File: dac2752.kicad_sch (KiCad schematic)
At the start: 24 parts, among them U30 LTC2752B, U301 OPA2197D, U31 OPA2189DGK, U32 OPA2388DGK, U34 OPA2388DGK

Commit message: Progress checkin.  About to redo FDA feedback again.
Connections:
- net Alt: now also R316.1; no longer R316.2
- net Force: now also C303.1; no longer C303.2
- net GND: now also R309.2; no longer R309.1
- net IOUT1: now also C303.2; no longer C303.1
- net at C304.2, U32.6 (-): now also R309.1; no longer R309.2
- net at C311.1, R315.1, U31.3 (+): now also R316.2; no longer R316.1
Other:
- moved on the sheet: C303, R309, R316
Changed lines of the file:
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@@
 	)
 	(junction
-		(at 170.18 118.11)
+		(at 144.78 81.28)
 		(diameter 0)
 		(color 0 0 0 0)
 	)
 	(junction
-		(at 110.49 81.28)
+		(at 170.18 118.11)
 		(diameter 0)
 		(color 0 0 0 0)
 	)
 	(junction
-		(at 153.67 100.33)
+		(at 110.49 81.28)
 		(diameter 0)
 		(color 0 0 0 0)
 	)
 	(junction
-		(at 102.87 101.6)
+		(at 153.67 100.33)
 		(diameter 0)
 		(color 0 0 0 0)
 	)
 	(junction
-		(at 144.78 81.28)
+		(at 102.87 101.6)
 		(diameter 0)
 		(color 0 0 0 0)
@@
 	)
 	(junction
-		(at 144.78 88.9)
-		(diameter 0)
-		(color 0 0 0 0)
-	)
-	(junction
 		(at 168.91 93.98)
 		(diameter 0)
@@
 	)
 	(junction
+		(at 144.78 88.9)
+		(diameter 0)
+		(color 0 0 0 0)
+	)
+	(junction
 		(at 73.66 76.2)
 		(diameter 0)
@@
 	(wire
 		(pts
-			(xy 144.78 81.28) (xy 194.31 81.28)
+			(xy 72.39 73.66) (xy 73.66 73.66)
 		)
 		(stroke
@@
 	(wire
 		(pts
-			(xy 72.39 73.66) (xy 73.66 73.66)
+			(xy 73.66 73.66) (xy 73.66 76.2)
 		)
 		(stroke
@@
 	(wire
 		(pts
-			(xy 73.66 73.66) (xy 73.66 76.2)
+			(xy 80.01 81.28) (xy 80.01 86.36)
 		)
 		(stroke
@@
 	(wire
 		(pts
-			(xy 80.01 81.28) (xy 80.01 86.36)
+			(xy 63.5 76.2) (xy 64.77 76.2)
 		)
 		(stroke
@@
 	(wire
 		(pts
-			(xy 63.5 76.2) (xy 64.77 76.2)
+			(xy 62.23 99.06) (xy 62.23 93.98)
 		)
 		(stroke
@@
 	(wire
 		(pts
-			(xy 62.23 99.06) (xy 62.23 93.98)
+			(xy 66.04 110.49) (xy 62.23 110.49)
 		)
 		(stroke
@@
 	(wire
 		(pts
-			(xy 66.04 110.49) (xy 62.23 110.49)
+			(xy 144.78 88.9) (xy 153.67 88.9)
 		)
 		(stroke
@@
 	(wire
 		(pts
+			(xy 144.78 81.28) (xy 194.31 81.28)
+		)
+		(stroke
+			(width 0)
+			(type default)
+		)
+	)
+	(wire
+		(pts
 			(xy 102.87 93.98) (xy 110.49 93.98)
 		)
@@
 	(wire
 		(pts
-			(xy 144.78 88.9) (xy 153.67 88.9)
-		)
-		(stroke
-			(width 0)
-			(type default)
-		)
-	)
-	(wire
-		(pts
 			(xy 102.87 101.6) (xy 102.87 110.49)
 		)
@@
 		(lib_id "Device:C")
 		(at 170.18 114.3 0)
-		(mirror y)
 		(unit 1)
 		(exclude_from_sim no)
@@
 					(size 1.27 1.27)
 				)
-				(justify right)
+				(justify left)
 			)
 		)
@@
 					(size 1.27 1.27)
 				)
-				(justify right top)
+				(justify left top)
 			)
 		)
 		(property "Footprint" "Capacitor_SMD:C_0402_1005Metric"
-			(at 169.2148 118.11 0)
+			(at 171.1452 118.11 0)
 			(effects
 				(font
@@
 		(dnp no)
 		(property "Reference" "R303"
-			(at 82.55 106.172 90)
+			(at 82.55 102.108 90)
 			(effects
 				(font
@@
 		(lib_id "Device:R")
 		(at 57.15 110.49 270)
-		(mirror x)
 		(unit 1)
 		(exclude_from_sim no)
@@
 		(dnp no)
 		(property "Reference" "R301"
-			(at 57.15 108.458 90)
+			(at 57.15 112.522 90)
 			(effects
 				(font
@@
 		)
 		(property "Footprint" "Resistor_SMD:R_0402_1005Metric"
-			(at 57.15 112.268 90)
+			(at 57.15 108.712 90)
 			(effects
 				(font
@@
 		(lib_id "Device:C")
 		(at 185.42 114.3 0)
-		(mirror y)
 		(unit 1)
 		(exclude_from_sim no)
@@
 					(size 1.27 1.27)
 				)
-				(justify left)
+				(justify right)
 			)
 		)
@@
 					(size 1.27 1.27)
 				)
-				(justify left top)
+				(justify right top)
 			)
 		)
 		(property "Footprint" "Capacitor_SMD:C_0402_1005Metric"
-			(at 184.4548 118.11 0)
+			(at 186.3852 118.11 0)
 			(effects
 				(font
@@
 		(lib_id "Device:C")
 		(at 69.85 110.49 270)
-		(mirror x)
 		(unit 1)
 		(exclude_from_sim no)
@@
 		)
 		(property "Footprint" "Capacitor_SMD:C_0603_1608Metric"
-			(at 66.04 109.5248 0)
+			(at 66.04 111.4552 0)
 			(effects
 				(font
@@
 	(symbol
 		(lib_id "Device:C")
-		(at 144.78 85.09 180)
+		(at 144.78 85.09 0)
 		(unit 1)
 		(exclude_from_sim no)
@@
 		(dnp no)
 		(property "Reference" "C303"
-			(at 144.78 83.058 0)
+			(at 144.78 82.804 0)
 			(effects
 				(font
@@
 		)
 		(property "Value" "330p"
-			(at 144.78 83.058 0)
+			(at 144.78 82.804 0)
 			(effects
 				(font
@@
 		)
 		(property "Footprint" "Capacitor_SMD:C_0603_1608Metric"
-			(at 143.8148 81.28 0)
+			(at 145.7452 88.9 0)
 			(effects
 				(font
@@
 	(symbol
 		(lib_id "Device:R")
-		(at 68.58 73.66 270)
-		(mirror x)
+		(at 68.58 73.66 90)
 		(unit 1)
 		(exclude_from_sim no)
@@
 		(lib_id "Device:C")
 		(at 170.18 121.92 0)
-		(mirror y)
 		(unit 1)
 		(exclude_from_sim no)
@@
 					(size 1.27 1.27)
 				)
-				(justify right)
+				(justify left)
 			)
 		)
@@
 					(size 1.27 1.27)
 				)
-				(justify right top)
+				(justify left top)
 			)
 		)
 		(property "Footprint" "Capacitor_SMD:C_0402_1005Metric"
-			(at 169.2148 125.73 0)
+			(at 171.1452 125.73 0)
 			(effects
 				(font
@@
 	(symbol
 		(lib_id "Device:R")
-		(at 153.67 105.41 180)
+		(at 153.67 105.41 0)
 		(unit 1)
 		(exclude_from_sim no)
@@
 		)
 		(property "Footprint" "Resistor_SMD:R_0402_1005Metric"
-			(at 155.448 105.41 90)
+			(at 151.892 105.41 90)
 			(effects
 				(font
@@
 		(lib_id "Device:R")
 		(at 173.99 93.98 270)
-		(mirror x)
 		(unit 1)
 		(exclude_from_sim no)
@@
 		)
 		(property "Footprint" "Resistor_SMD:R_0402_1005Metric"
-			(at 173.99 95.758 90)
+			(at 173.99 92.202 90)
 			(effects
 				(font
@@
 		(lib_id "Device:R")
 		(at 68.58 76.2 270)
-		(mirror x)
 		(unit 1)
 		(exclude_from_sim no)
@@
 		)
 		(property "Footprint" "Resistor_SMD:R_0603_1608Metric"
-			(at 68.58 77.978 90)
+			(at 68.58 74.422 90)
 			(effects
 				(font
@@
 		(lib_id "Device:C")
 		(at 161.29 100.33 270)
-		(mirror x)
 		(unit 1)
 		(exclude_from_sim no)
@@
 		)
 		(property "Footprint" "Capacitor_SMD:C_0603_1608Metric"
-			(at 157.48 99.3648 0)
+			(at 157.48 101.2952 0)
 			(effects
 				(font
@@
 		(lib_id "Device:C")
 		(at 185.42 121.92 0)
-		(mirror y)
 		(unit 1)
 		(exclude_from_sim no)
@@
 					(size 1.27 1.27)
 				)
-				(justify left)
+				(justify right)
 			)
 		)
@@
 					(size 1.27 1.27)
 				)
-				(justify left top)
+				(justify right top)
 			)
 		)
 		(property "Footprint" "Capacitor_SMD:C_0402_1005Metric"
-			(at 184.4548 125.73 0)
+			(at 186.3852 125.73 0)
 			(effects
 				(font

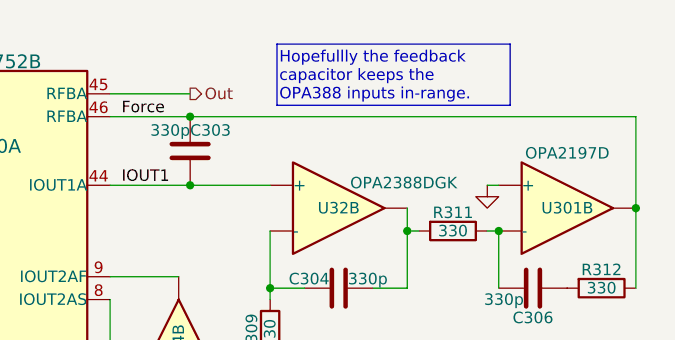
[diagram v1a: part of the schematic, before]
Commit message: Start to place within physical board size.
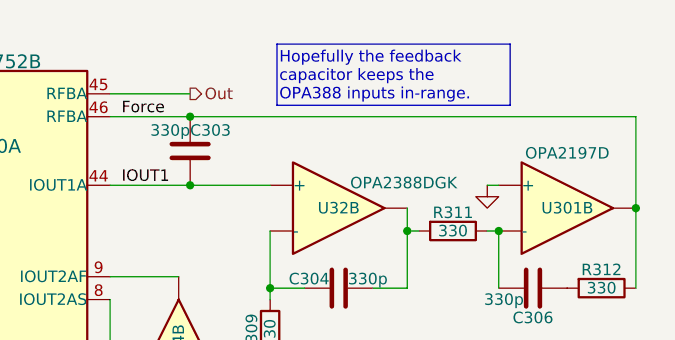
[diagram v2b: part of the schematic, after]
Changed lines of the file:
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@@
 	(generator_version "9.0")
 	(paper "A4")
-	(text_box "Hopefullly the feedback capacitor keeps the OPA388 inputs in-range."
+	(text_box "Hopefully the feedback capacitor keeps the OPA388 inputs in-range."
 		(exclude_from_sim no)
 		(at 154.4319 73.2099 0)

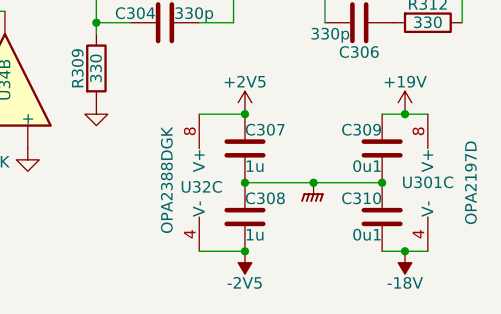
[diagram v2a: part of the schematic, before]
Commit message: Power mostly routed
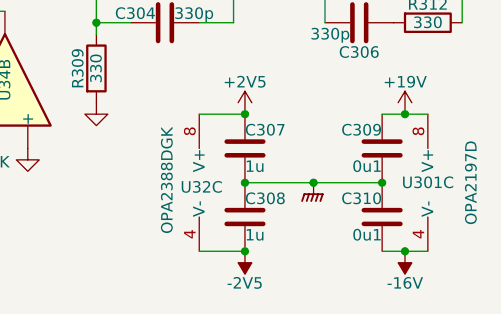
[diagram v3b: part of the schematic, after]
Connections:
- net -18V renamed -16V
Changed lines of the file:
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@@
 				)
 				(path "/b054cef4-39e3-49d8-aff0-7ba5a206c187/aeb3a378-4287-41b1-9e33-8dbd035c4d66"
-					(reference "C367")
+					(reference "C366")
 					(unit 1)
 				)
@@
 				)
 				(path "/b054cef4-39e3-49d8-aff0-7ba5a206c187/aeb3a378-4287-41b1-9e33-8dbd035c4d66"
-					(reference "C369")
+					(reference "C368")
 					(unit 1)
 				)
@@
 				)
 				(path "/b054cef4-39e3-49d8-aff0-7ba5a206c187/aeb3a378-4287-41b1-9e33-8dbd035c4d66"
-					(reference "C366")
+					(reference "C365")
 					(unit 1)
 				)
@@
 				)
 				(path "/b054cef4-39e3-49d8-aff0-7ba5a206c187/aeb3a378-4287-41b1-9e33-8dbd035c4d66"
-					(reference "C368")
+					(reference "C367")
 					(unit 1)
 				)
@@
 				)
 				(path "/b054cef4-39e3-49d8-aff0-7ba5a206c187/aeb3a378-4287-41b1-9e33-8dbd035c4d66"
-					(reference "C370")
+					(reference "C369")
 					(unit 1)
 				)
@@
 	)
 	(symbol
-		(lib_id "External:-18V")
+		(lib_id "Parts:-16V")
 		(at 187.96 125.73 0)
 		(mirror y)
@@
 			)
 		)
-		(property "Value" "-18V"
+		(property "Value" "-16V"
 			(at 187.96 129.286 0)
 			(do_not_autoplace yes)
@@
 			)
 		)
-		(property "Description" "Power symbol creates a global label with name \"-18V\""
+		(property "Description" "Power symbol creates a global label with name \"-16V\""
 			(at 187.96 125.73 0)
 			(effects

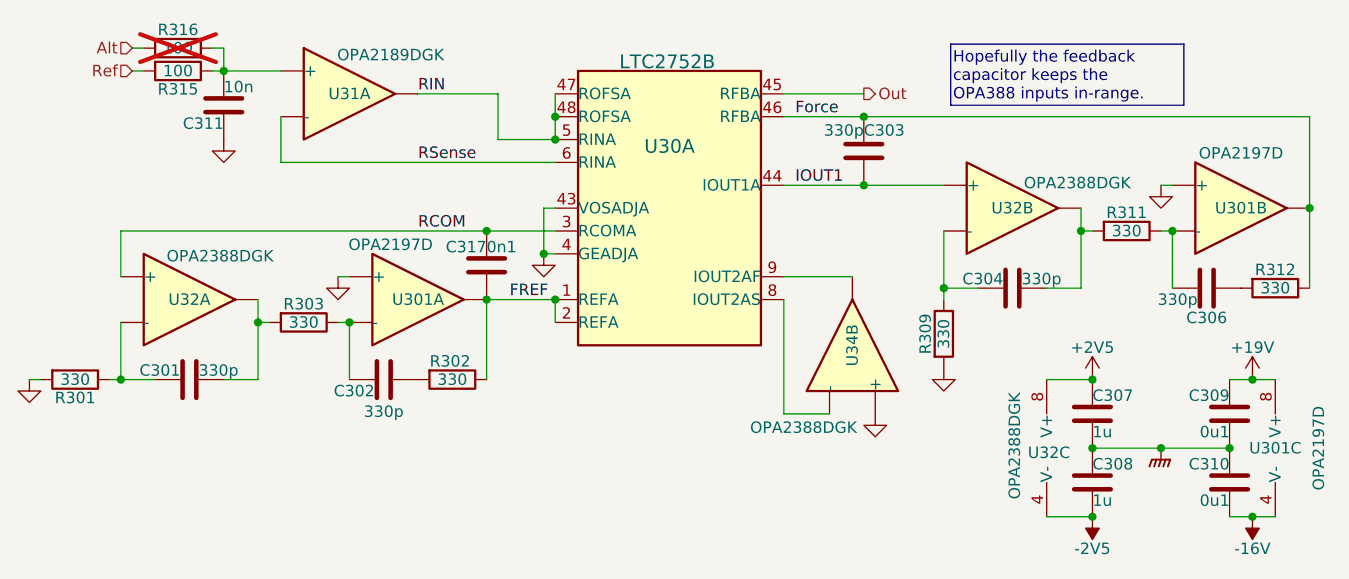
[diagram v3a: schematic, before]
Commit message: Nearly all routed.  Repinning FDA resistors.
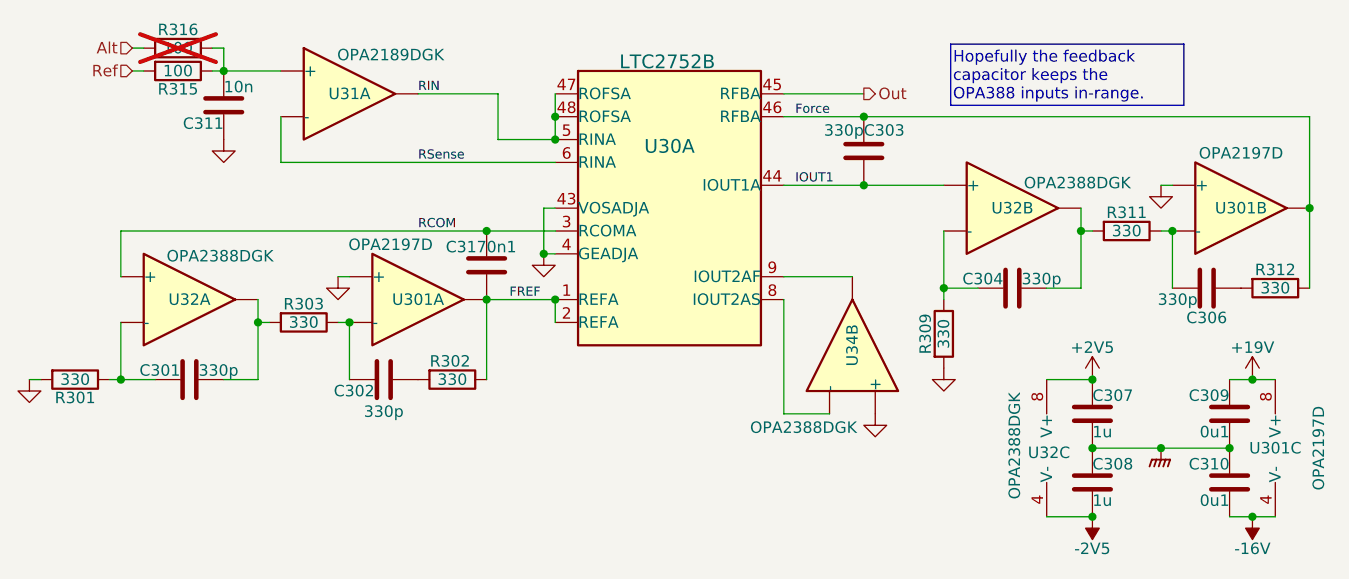
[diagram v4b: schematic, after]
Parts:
- C317: footprint Capacitor_SMD:C_0402_1005Metric -> Capacitor_SMD:C_0603_1608Metric; LCSC C1546 -> (none)
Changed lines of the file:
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@@
 		(effects
 			(font
-				(size 1.27 1.27)
+				(size 1.016 1.016)
 			)
 			(justify left bottom)
@@
 		(effects
 			(font
-				(size 1.27 1.27)
+				(size 1.016 1.016)
 			)
 			(justify left bottom)
@@
 		(effects
 			(font
-				(size 1.27 1.27)
+				(size 1.016 1.016)
 			)
 			(justify left bottom)
@@
 		(effects
 			(font
-				(size 1.27 1.27)
+				(size 1.016 1.016)
 			)
 			(justify left bottom)
@@
 		(effects
 			(font
-				(size 1.27 1.27)
+				(size 1.016 1.016)
 			)
 			(justify left bottom)
@@
 		(effects
 			(font
-				(size 1.27 1.27)
+				(size 1.016 1.016)
 			)
 			(justify left bottom)
@@
 			)
 		)
-		(property "Footprint" "Capacitor_SMD:C_0402_1005Metric"
+		(property "Footprint" "Capacitor_SMD:C_0603_1608Metric"
 			(at 103.8352 101.6 0)
 			(effects
@@
 			)
 		)
-		(property "LCSC" "C1546"
+		(property "LCSC" ""
 			(at 102.87 97.79 0)
 			(effects

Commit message: DRC update.  Repin ADC.  De-crack the S/H ground.
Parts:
- added R304: 100, Resistor_SMD:R_0402_1005Metric, symbol Device:R
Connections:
- net Force: now also R304.2; no longer U30.46 (RFBA)
- new net: R304.1, U30.46 (RFBA)
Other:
- moved on the sheet: C303
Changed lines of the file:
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@@
-	)
-	(junction
-		(at 144.78 81.28)
-		(diameter 0)
-		(color 0 0 0 0)
 	)
 	(junction
@@
 	)
 	(junction
+		(at 152.4 88.9)
+		(diameter 0)
+		(color 0 0 0 0)
+	)
+	(junction
+		(at 152.4 81.28)
+		(diameter 0)
+		(color 0 0 0 0)
+	)
+	(junction
 		(at 102.87 101.6)
 		(diameter 0)
@@
 	)
 	(junction
-		(at 144.78 88.9)
-		(diameter 0)
-		(color 0 0 0 0)
-	)
-	(junction
 		(at 73.66 76.2)
 		(diameter 0)
@@
 	(wire
 		(pts
-			(xy 144.78 88.9) (xy 153.67 88.9)
-		)
-		(stroke
-			(width 0)
-			(type default)
-		)
-	)
-	(wire
-		(pts
 			(xy 187.96 125.73) (xy 185.42 125.73)
 		)
@@
 	(wire
 		(pts
-			(xy 144.78 81.28) (xy 194.31 81.28)
-		)
-		(stroke
-			(width 0)
-			(type default)
-		)
-	)
-	(wire
-		(pts
 			(xy 102.87 93.98) (xy 110.49 93.98)
 		)
@@
 	(wire
 		(pts
-			(xy 135.89 81.28) (xy 144.78 81.28)
+			(xy 135.89 81.28) (xy 142.24 81.28)
 		)
 		(stroke
@@
 	(wire
 		(pts
+			(xy 152.4 88.9) (xy 153.67 88.9)
+		)
+		(stroke
+			(width 0)
+			(type default)
+		)
+	)
+	(wire
+		(pts
 			(xy 135.89 78.74) (xy 144.78 78.74)
 		)
@@
 	(wire
 		(pts
+			(xy 152.4 81.28) (xy 194.31 81.28)
+		)
+		(stroke
+			(width 0)
+			(type default)
+		)
+	)
+	(wire
+		(pts
 			(xy 52.07 110.49) (xy 53.34 110.49)
 		)
@@
 	(wire
 		(pts
-			(xy 135.89 88.9) (xy 144.78 88.9)
+			(xy 135.89 88.9) (xy 152.4 88.9)
 		)
 		(stroke
@@
 		(pts
 			(xy 165.1 110.49) (xy 170.18 110.49)
+		)
+		(stroke
+			(width 0)
+			(type default)
+		)
+	)
+	(wire
+		(pts
+			(xy 149.86 81.28) (xy 152.4 81.28)
 		)
 		(stroke
@@
 	)
 	(label "Force"
-		(at 137.16 81.28 0)
+		(at 181.61 81.28 0)
 		(effects
 			(font
@@
 				(path "/b054cef4-39e3-49d8-aff0-7ba5a206c187/f2e682f2-52ca-4ed0-8a7d-aeb09fbc9914"
 					(reference "R302")
+					(unit 1)
+				)
+			)
+		)
+	)
+	(symbol
+		(lib_id "Device:R")
+		(at 146.05 81.28 90)
+		(unit 1)
+		(exclude_from_sim no)
+		(in_bom yes)
+		(on_board yes)
+		(dnp no)
+		(property "Reference" "R304"
+			(at 146.05 83.312 90)
+			(effects
+				(font
+					(size 1.27 1.27)
+				)
+			)
+		)
+		(property "Value" "100"
+			(at 146.05 81.28 90)
+			(effects
+				(font
+					(size 1.27 1.27)
+				)
+			)
+		)
+		(property "Footprint" "Resistor_SMD:R_0402_1005Metric"
+			(at 146.05 83.058 90)
+			(effects
+				(font
+					(size 1.27 1.27)
+				)
+				(hide yes)
+			)
+		)
+		(property "Datasheet" "~"
+			(at 146.05 81.28 0)
+			(effects
+				(font
+					(size 1.27 1.27)
+				)
+				(hide yes)
+			)
+		)
+		(property "Description" "Resistor"
+			(at 146.05 81.28 0)
+			(effects
+				(font
+					(size 1.27 1.27)
+				)
+				(hide yes)
+			)
+		)
+		(property "LCSC" "C25076"
+			(at 146.05 81.28 90)
+			(effects
+				(font
+					(size 1.27 1.27)
+				)
+				(hide yes)
+			)
+		)
+		(property "Stock" ""
+			(at 146.05 81.28 90)
+			(effects
+				(font
+					(size 1.27 1.27)
+				)
+				(hide yes)
+			)
+		)
+		(pin "2"
+		)
+		(pin "1"
+		)
+		(instances
+			(project "lincal"
+				(path "/b054cef4-39e3-49d8-aff0-7ba5a206c187/361a423f-d05f-4f8b-bc28-600b62434109"
+					(reference "R324")
+					(unit 1)
+				)
+				(path "/b054cef4-39e3-49d8-aff0-7ba5a206c187/460d889b-fb9b-4b3e-8128-6fba79ce7ab4"
+					(reference "R344")
+					(unit 1)
+				)
+				(path "/b054cef4-39e3-49d8-aff0-7ba5a206c187/aeb3a378-4287-41b1-9e33-8dbd035c4d66"
+					(reference "R364")
+					(unit 1)
+				)
+				(path "/b054cef4-39e3-49d8-aff0-7ba5a206c187/f2e682f2-52ca-4ed0-8a7d-aeb09fbc9914"
+					(reference "R304")
 					(unit 1)
 				)
@@
 	(symbol
 		(lib_id "Device:C")
-		(at 144.78 85.09 0)
+		(at 152.4 85.09 0)
 		(unit 1)
 		(exclude_from_sim no)
@@
 		(dnp no)
 		(property "Reference" "C303"
-			(at 144.78 82.804 0)
+			(at 152.4 82.804 0)
 			(effects
 				(font
@@
 		)
 		(property "Value" "330p"
-			(at 144.78 82.804 0)
+			(at 152.4 87.122 0)
 			(effects
 				(font
@@
 		)
 		(property "Footprint" "Capacitor_SMD:C_0603_1608Metric"
-			(at 145.7452 88.9 0)
+			(at 153.3652 88.9 0)
 			(effects
 				(font
@@
 		)
 		(property "Datasheet" "C0G, 50V"
-			(at 144.78 85.09 0)
+			(at 152.4 85.09 0)
 			(effects
 				(font
@@
 		)
 		(property "Description" "Unpolarized capacitor"
-			(at 144.78 85.09 0)
+			(at 152.4 85.09 0)
 			(effects
 				(font
@@
 		)
 		(property "LCSC" "C1664"
-			(at 144.78 85.09 0)
+			(at 152.4 85.09 0)
 			(effects
 				(font
@@
 		)
 		(property "Stock" ""
-			(at 144.78 85.09 90)
-			(effects
-				(font
+			(at 152.4 85.09 90)
+			(effects
+				(font

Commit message: More component metadata.
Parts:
- C301, C302, C303, C304, C306, C307, C308, C309, C310, C311, R301, R302, R303, R304, R309, R311, R312, R315, U30: Stock (none) -> JLC
- C317: LCSC (none) -> C14858; Stock (none) -> JLC
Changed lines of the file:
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@@
 			)
 		)
-		(property "Stock" ""
+		(property "Stock" "JLC"
 			(at 170.18 114.3 0)
 			(effects
@@
 			)
 		)
-		(property "Stock" ""
+		(property "Stock" "JLC"
 			(at 82.55 104.14 90)
 			(effects
@@
 			)
 		)
-		(property "Stock" ""
+		(property "Stock" "JLC"
 			(at 91.44 110.49 90)
 			(effects
@@
 			)
 		)
-		(property "LCSC" ""
+		(property "LCSC" "C14858"
 			(at 102.87 97.79 0)
 			(effects
@@
 			)
 		)
-		(property "Stock" ""
+		(property "Stock" "JLC"
 			(at 102.87 97.79 0)
 			(effects
@@
 			)
 		)
-		(property "Stock" ""
+		(property "Stock" "JLC"
 			(at 99.06 110.49 90)
 			(effects
@@
 			)
 		)
-		(property "Stock" ""
+		(property "Stock" "JLC"
 			(at 146.05 81.28 90)
 			(effects
@@
 			)
 		)
-		(property "Stock" ""
+		(property "Stock" "JLC"
 			(at 123.19 91.44 0)
 			(effects
@@
 			)
 		)
-		(property "Stock" ""
+		(property "Stock" "JLC"
 			(at 57.15 110.49 90)
 			(effects
@@
 			)
 		)
-		(property "Stock" ""
+		(property "Stock" "JLC"
 			(at 185.42 114.3 0)
 			(effects
@@
 			)
 		)
-		(property "Stock" ""
+		(property "Stock" "JLC"
 			(at 69.85 110.49 90)
 			(effects
@@
 			)
 		)
-		(property "Stock" ""
+		(property "Stock" "JLC"
 			(at 190.5 100.33 90)
 			(effects
@@
 			)
 		)
-		(property "Stock" ""
+		(property "Stock" "JLC"
 			(at 152.4 85.09 90)
 			(effects
@@
 			)
 		)
-		(property "Stock" ""
+		(property "Stock" "JLC"
 			(at 182.88 100.33 90)
 			(effects
@@
 			)
 		)
-		(property "Stock" ""
+		(property "Stock" "JLC"
 			(at 170.18 121.92 0)
 			(effects
@@
 			)
 		)
-		(property "Stock" ""
+		(property "Stock" "JLC"
 			(at 153.67 105.41 90)
 			(effects
@@
 			)
 		)
-		(property "Stock" ""
+		(property "Stock" "JLC"
 			(at 73.66 80.01 0)
 			(effects
@@
 			)
 		)
-		(property "Stock" ""
+		(property "Stock" "JLC"
 			(at 173.99 93.98 90)
 			(effects
@@
 			)
 		)
-		(property "Stock" ""
+		(property "Stock" "JLC"
 			(at 68.58 76.2 90)
 			(effects
@@
 			)
 		)
-		(property "Stock" ""
+		(property "Stock" "JLC"
 			(at 161.29 100.33 90)
 			(effects
@@
 			)
 		)
-		(property "Stock" ""
+		(property "Stock" "JLC"
 			(at 185.42 121.92 0)
 			(effects

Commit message: Front panel
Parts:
- C317: value 0n1 -> 330p; LCSC C14858 -> C1664
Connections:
- net GND: no longer U30.4 (GEADJA)
- net at U30.9 (IOUT2AF), U34.7: now also U30.4 (GEADJA)
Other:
- moved on the sheet: C307, C308, C309, C310, U301C, U32C, U34B
